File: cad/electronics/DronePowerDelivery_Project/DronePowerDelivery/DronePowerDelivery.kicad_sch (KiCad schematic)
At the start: 0 parts

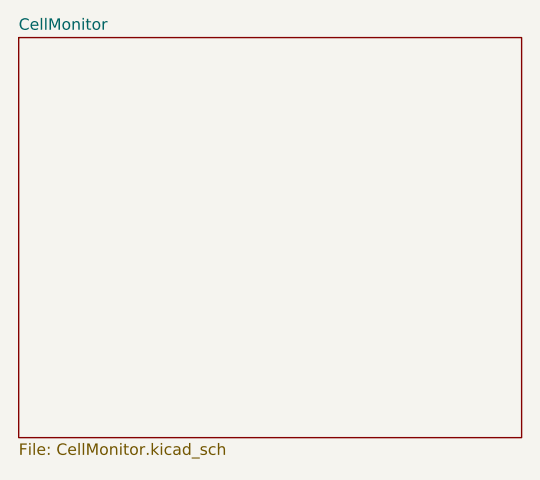
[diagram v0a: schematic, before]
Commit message: Added additional schematic capture
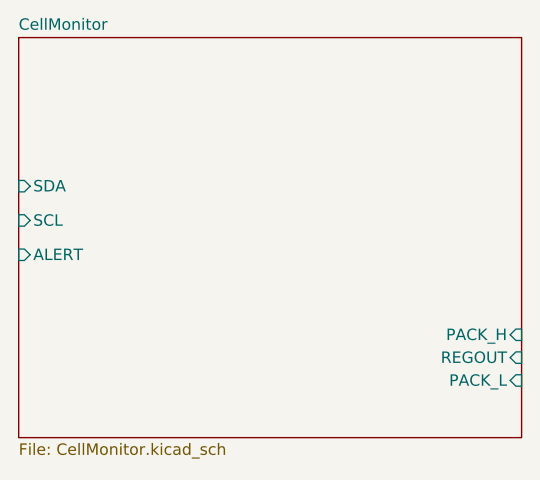
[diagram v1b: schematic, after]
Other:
- sheet CellMonitor ports: added ALERT, PACK_H, PACK_L, REGOUT, SCL, SDA; removed none
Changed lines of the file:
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@@
       (effects (font (size 1.27 1.27)) (justify left top))
+    )
+    (pin "PACK_L" input (at 209.55 93.98 0)
+      (effects (font (size 1.27 1.27)) (justify right))
+    )
+    (pin "ALERT" input (at 153.67 80.01 180)
+      (effects (font (size 1.27 1.27)) (justify left))
+    )
+    (pin "PACK_H" input (at 209.55 88.9 0)
+      (effects (font (size 1.27 1.27)) (justify right))
+    )
+    (pin "REGOUT" input (at 209.55 91.44 0)
+      (effects (font (size 1.27 1.27)) (justify right))
+    )
+    (pin "SCL" input (at 153.67 76.2 180)
+      (effects (font (size 1.27 1.27)) (justify left))
+    )
+    (pin "SDA" input (at 153.67 72.39 180)
+      (effects (font (size 1.27 1.27)) (justify left))
     )
     (instances

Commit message: Finialized Component Sizing
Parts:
- added J3: Conn_01x04_Pin, Connector_JST:JST_PH_B4B-PH-K_1x04_P2.00mm_Vertical, symbol Connector:Conn_01x04_Pin
- added J4: Conn_01x02_Socket, Connector_AMASS:AMASS_XT60-M_1x02_P7.20mm_Vertical, symbol Connector:Conn_01x02_Socket
- added TP1, TP2, TP3, TP4, TP5, TP6: TestPoint, TestPoint:TestPoint_Pad_3.0x3.0mm, symbol Connector:TestPoint
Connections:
- new net ALERT: J3.2 (Pin_2), TP4.1
- new net GNDREF: J3.4 (Pin_4), TP2.1, TP6.1
- new net PACK_H: J4.2 (Pin_2)
- new net PACK_L: J4.1 (Pin_1)
- new net REGOUT: TP1.1
- new net SCL: J3.1 (Pin_1), TP3.1
- new net SDA: J3.3 (Pin_3), TP5.1
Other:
- sheet CellMonitor ports: added GNDREF; removed none

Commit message: Rev.1 of PCB laid out
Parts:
- TP1, TP2, TP3, TP4, TP5, TP6: footprint TestPoint:TestPoint_Pad_3.0x3.0mm -> TestPoint:TestPoint_Pad_2.0x2.0mm
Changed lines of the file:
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@@
 (kicad_sch (version 20230121) (generator eeschema)
   (paper "A4")
+  (bus_alias "Connector" (members "SCL" "ALERT" "SDA" "GNDREF"))
   (bus_alias "Output" (members "PACK_H" "PACK_L" "REGOUT" "GNDREF"))
-  (bus_alias "Connector" (members "SCL" "ALERT" "SDA" "GNDREF"))
   (junction (at 72.39 86.36) (diameter 0) (color 0 0 0 0)
   )
@@
     (effects (font (size 1.27 1.27)) (justify right bottom))
   )
+  (netclass_flag "" (length 2.54) (shape round) (at 222.25 91.44 0) (fields_autoplaced)
+    (effects (font (size 1.27 1.27)) (justify left bottom))
+    (property "Netclass" "Power" (at 222.9485 88.9 0)
+      (effects (font (size 1.27 1.27) italic) (justify left))
+    )
+  )
+  (netclass_flag "" (length 2.54) (shape round) (at 222.25 93.98 180) (fields_autoplaced)
+    (effects (font (size 1.27 1.27)) (justify right bottom))
+    (property "Netclass" "Power" (at 222.9485 96.52 0)
+      (effects (font (size 1.27 1.27) italic) (justify left))
+    )
+  )
   (symbol (lib_id "Connector:TestPoint") (at 69.85 77.47 0) (unit 1)
     (in_bom yes) (on_board yes) (dnp no) (fields_autoplaced)
@@
       (effects (font (size 1.27 1.27)) (justify left))
     )
-    (property "Footprint" "TestPoint:TestPoint_Pad_3.0x3.0mm" (at 74.93 77.47 0)
+    (property "Footprint" "TestPoint:TestPoint_Pad_2.0x2.0mm" (at 74.93 77.47 0)
       (effects (font (size 1.27 1.27)) hide)
     )
@@
       (effects (font (size 1.27 1.27)) (justify right))
     )
-    (property "Footprint" "TestPoint:TestPoint_Pad_3.0x3.0mm" (at 67.31 99.06 0)
+    (property "Footprint" "TestPoint:TestPoint_Pad_2.0x2.0mm" (at 67.31 99.06 0)
       (effects (font (size 1.27 1.27)) hide)
     )
@@
       (effects (font (size 1.27 1.27)) (justify left))
     )
-    (property "Footprint" "TestPoint:TestPoint_Pad_3.0x3.0mm" (at 224.79 110.49 0)
+    (property "Footprint" "TestPoint:TestPoint_Pad_2.0x2.0mm" (at 224.79 110.49 0)
       (effects (font (size 1.27 1.27)) hide)
     )
@@
       (effects (font (size 1.27 1.27)) (justify right))
     )
-    (property "Footprint" "TestPoint:TestPoint_Pad_3.0x3.0mm" (at 64.77 102.87 0)
+    (property "Footprint" "TestPoint:TestPoint_Pad_2.0x2.0mm" (at 64.77 102.87 0)
       (effects (font (size 1.27 1.27)) hide)
     )
@@
       (effects (font (size 1.27 1.27)) (justify left))
     )
-    (property "Footprint" "TestPoint:TestPoint_Pad_3.0x3.0mm" (at 224.79 105.41 0)
+    (property "Footprint" "TestPoint:TestPoint_Pad_2.0x2.0mm" (at 224.79 105.41 0)
       (effects (font (size 1.27 1.27)) hide)
     )
@@
       (effects (font (size 1.27 1.27)) (justify left))
     )
-    (property "Footprint" "TestPoint:TestPoint_Pad_3.0x3.0mm" (at 77.47 81.28 0)
-      (effects (font (size 1.27 1.27)) hide)
-    )
+    (property "Footprint" "TestPoint:TestPoint_Pad_2.0x2.0mm" (at 77.47 81.28 0)
+      (effects (font (size 1.27 1.27)) hide)
+    )
